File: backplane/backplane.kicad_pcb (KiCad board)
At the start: 2 copper layers, 150 x 150 mm, 14 parts

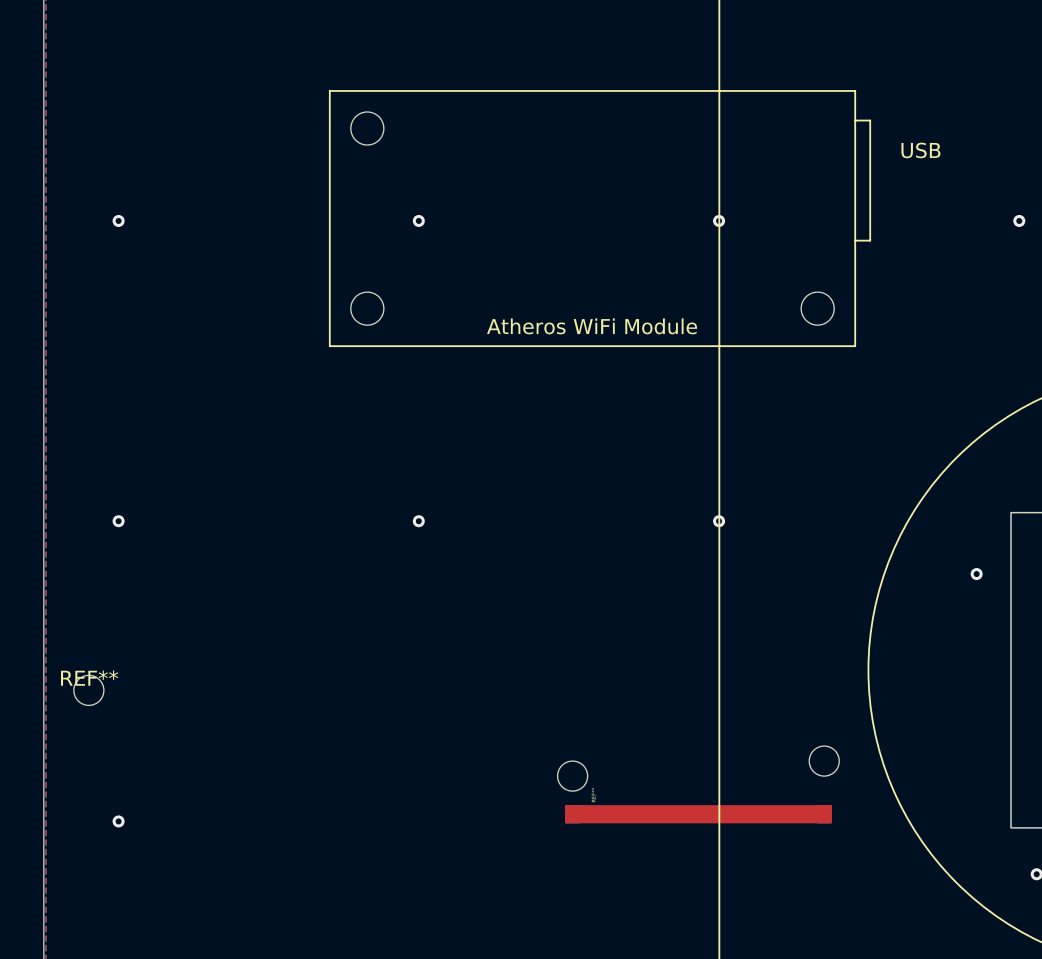
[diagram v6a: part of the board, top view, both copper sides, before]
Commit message: Adding major changes to transformer and others
Moved Atheros module out from under phone clamp for easier assembly.
Slot for antenna wire to feed through is now a edge cut.
Through-hole to GND plane on opposite end of transformer is now a SMD for
   a UFL connector.
Transformer clearance is now a copper trace isolating the microstrip.
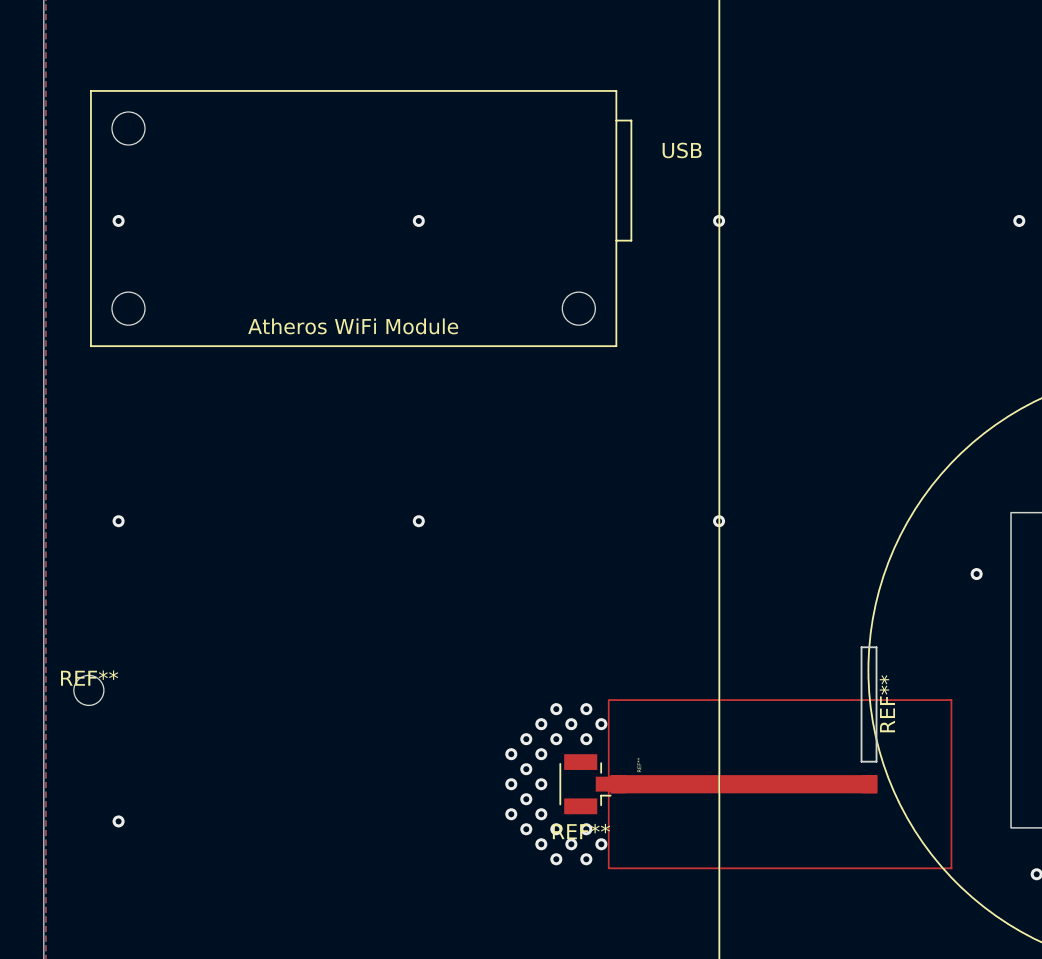
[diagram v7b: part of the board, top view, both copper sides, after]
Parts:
- added REF**: antenna-wire-slot, DxWiFi:antenna-wire-slot, F.Cu at (79.6, 107.7)
- added REF**: U.FL_Hirose_U.FL-R-SMT-1_Vertical, Connector_Coaxial:U.FL_Hirose_U.FL-R-SMT-1_Vertical, F.Cu at (59.1, 113.0)
- moved Atheros WiFi Module 15.9 mm to (26.0, 83.8)
- moved REF** 3.63 mm to (63.0, 113.0)
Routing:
- net Net-(L1-Pad1): vias 62 -> 86
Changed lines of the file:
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@@
     (thickness 1.6)
     (drawings 4)
-    (tracks 62)
+    (tracks 86)
     (zones 0)
-    (modules 14)
+    (modules 16)
     (nets 2)
   )
@@
     (mod_text_size 1 1)
     (mod_text_width 0.15)
-    (pad_size 0.8 0.8)
-    (pad_drill 0.4)
+    (pad_size 2.2 1.05)
+    (pad_drill 0)
     (pad_to_mask_clearance 0.051)
     (solder_mask_min_width 0.25)
@@
     (add_net "Net-(L1-Pad1)")
   )
-  (module muwave_stub (layer F.Cu)
-    (at 60 115 270)
-    (fp_text reference REF** (at -1.27 0.5 270) (layer F.SilkS)
+  (module DxWiFi:antenna-wire-slot (layer F.Cu)
+    (at 79.6 107.69 270)
+    (fp_text reference REF** (at 0 0.5 270) (layer F.SilkS)
+      (effects (font (size 1 1) (thickness 0.15)))
+    )
+    (fp_text value antenna-wire-slot (at 0 -0.5 270) (layer F.Fab)
+      (effects (font (size 1 1) (thickness 0.15)))
+    )
+    (fp_line (start 3.81 2.27) (end -3.81 2.27) (layer Edge.Cuts) (width 0.12))
+    (fp_line (start 3.81 1.27) (end 3.81 2.27) (layer Edge.Cuts) (width 0.12))
+    (fp_line (start -3.81 1.27) (end 3.81 1.27) (layer Edge.Cuts) (width 0.12))
+    (fp_line (start -3.81 1.27) (end -3.81 2.27) (layer Edge.Cuts) (width 0.12))
+  )
+  (module muwave_stub locked (layer F.Cu)
+    (at 63.03385 113 270)
+    (fp_text reference REF** (at -1.27 0.5 90) (layer F.SilkS)
       (effects (font (size 0.25 0.25) (thickness 0.05)))
     )
-    (fp_text value muwave_stub (at 0 -0.5 270) (layer F.Fab)
+    (fp_text value muwave_stub (at 0 -0.5 90) (layer F.Fab)
       (effects (font (size 0.25 0.25) (thickness 0.05)))
     )
-    (pad "" np_thru_hole circle (at -2.54 1.915 270) (size 2 2) (drill 2) (layers *.Cu *.Mask))
-    (pad "" np_thru_hole roundrect (at -3.54 -14.8473 270) (size 4 2) (drill 2) (layers *.Cu) (roundrect_rratio 0.25)
-      (clearance 0.5))
-    (pad 2 smd rect (at 0 1.915 270) (size 1.20938 1) (layers F.Cu F.Mask))
-    (pad 2 smd rect (at 0 -14.8473 270) (size 1.20938 1) (layers F.Cu F.Mask))
-    (pad 1 smd rect (at 0 0 270) (size 0.25 0.25) (layers B.Cu))
-    (pad 1 smd rect (at 0 -6.46615 270) (size 1.20938 17.7623) (layers F.Cu)
-      (clearance 12.6))
+    (fp_line (start -5.60469 2.54) (end 5.60469 2.54) (layer F.Cu) (width 0.12))
+    (fp_line (start 5.60469 -20.287299) (end 5.60469 2.475001) (layer F.Cu) (width 0.12))
+    (fp_line (start -5.60469 -20.287299) (end 5.60469 -20.287299) (layer F.Cu) (width 0.12))
+    (fp_line (start -5.60469 -20.287299) (end -5.60469 2.475001) (layer F.Cu) (width 0.12))
+    (pad 1 smd rect (at 0 -6.46615 270) (size 1.20938 17.7623) (layers F.Cu))
+    (pad 1 smd rect (at 0 -14.8473 270) (size 1.20938 1) (layers F.Cu F.Mask))
+    (pad 1 smd rect (at 0 1.915 270) (size 1.20938 1) (layers F.Cu F.Mask))
+  )
+  (module Connector_Coaxial:U.FL_Hirose_U.FL-R-SMT-1_Vertical (layer F.Cu)
+    (at 59.1 113 180)
+    (descr "Hirose U.FL Coaxial https://www.hirose.com/product/en/products/U.FL/U.FL-R-SMT-1%2810%29/")
+    (tags "Hirose U.FL Coaxial")
+    (attr smd)
+    (fp_text reference REF** (at 0.475 -3.2) (layer F.SilkS)
+      (effects (font (size 1 1) (thickness 0.15)))
+    )
+    (fp_text value U.FL_Hirose_U.FL-R-SMT-1_Vertical (at 0.475 3.2) (layer F.Fab)
+      (effects (font (size 1 1) (thickness 0.15)))
+    )
+    (fp_line (start -1.32 -1) (end -2.02 -1) (layer F.CrtYd) (width 0.05))
+    (fp_line (start -1.32 1.8) (end -1.32 1) (layer F.CrtYd) (width 0.05))
+    (fp_line (start -1.32 -1.8) (end -1.12 -1.8) (layer F.CrtYd) (width 0.05))
+    (fp_line (start -1.12 -1.8) (end -1.12 -2.5) (layer F.CrtYd) (width 0.05))
+    (fp_line (start 2.08 -2.5) (end -1.12 -2.5) (layer F.CrtYd) (width 0.05))
+    (fp_line (start -1.32 -1) (end -1.32 -1.8) (layer F.CrtYd) (width 0.05))
+    (fp_line (start 2.08 -1.8) (end 2.08 -2.5) (layer F.CrtYd) (width 0.05))
+    (fp_line (start 2.08 -1.8) (end 2.28 -1.8) (layer F.CrtYd) (width 0.05))
+    (fp_line (start -0.885 -1.4) (end -0.885 -0.76) (layer F.SilkS) (width 0.12))
+    (fp_line (start -0.425 1.5) (end -0.425 1.3) (layer F.Fab) (width 0.1))
+    (fp_line (start -0.425 1.3) (end -0.825 1.3) (layer F.Fab) (width 0.1))
+    (fp_line (start -0.825 0.3) (end -0.825 1.3) (layer F.Fab) (width 0.1))
+    (fp_line (start -1.075 0.3) (end -0.825 0.3) (layer F.Fab) (width 0.1))
+    (fp_line (start -1.075 0.3) (end -1.075 -0.15) (layer F.Fab) (width 0.1))
+    (fp_line (start -0.925 -0.3) (end -0.825 -0.3) (layer F.Fab) (width 0.1))
+    (fp_line (start -0.825 -0.3) (end -0.825 -1.3) (layer F.Fab) (width 0.1))
+    (fp_line (start -0.425 -1.5) (end -0.425 -1.3) (layer F.Fab) (width 0.1))
+    (fp_line (start -0.425 -1.3) (end -0.825 -1.3) (layer F.Fab) (width 0.1))
+    (fp_line (start -0.425 1.5) (end 1.375 1.5) (layer F.Fab) (width 0.1))
+    (fp_line (start 1.375 1.5) (end 1.375 1.3) (layer F.Fab) (width 0.1))
+    (fp_line (start 1.775 1.3) (end 1.375 1.3) (layer F.Fab) (width 0.1))
+    (fp_line (start 1.775 -1.3) (end 1.775 1.3) (layer F.Fab) (width 0.1))
+    (fp_line (start -0.425 -1.5) (end 1.375 -1.5) (layer F.Fab) (width 0.1))
+    (fp_line (start 1.375 -1.5) (end 1.375 -1.3) (layer F.Fab) (width 0.1))
+    (fp_line (start 1.775 -1.3) (end 1.375 -1.3) (layer F.Fab) (width 0.1))
+    (fp_line (start -0.925 -0.3) (end -1.075 -0.15) (layer F.Fab) (width 0.1))
+    (fp_line (start -0.885 1.4) (end -0.885 0.76) (layer F.SilkS) (width 0.12))
+    (fp_line (start -0.885 -0.76) (end -1.515 -0.76) (layer F.SilkS) (width 0.12))
+    (fp_line (start 1.835 -1.35) (end 1.835 1.35) (layer F.SilkS) (width 0.12))
+    (fp_line (start 2.08 2.5) (end -1.12 2.5) (layer F.CrtYd) (width 0.05))
+    (fp_line (start -1.12 2.5) (end -1.12 1.8) (layer F.CrtYd) (width 0.05))
+    (fp_line (start -1.32 1.8) (end -1.12 1.8) (layer F.CrtYd) (width 0.05))
+    (fp_line (start 2.28 1.8) (end 2.28 -1.8) (layer F.CrtYd) (width 0.05))
+    (fp_line (start 2.08 2.5) (end 2.08 1.8) (layer F.CrtYd) (width 0.05))
+    (fp_line (start 2.08 1.8) (end 2.28 1.8) (layer F.CrtYd) (width 0.05))
+    (fp_line (start -1.32 1) (end -2.02 1) (layer F.CrtYd) (width 0.05))
+    (fp_line (start -2.02 1) (end -2.02 -1) (layer F.CrtYd) (width 0.05))
+    (fp_text user %R (at 0.475 0 90) (layer F.Fab)
+      (effects (font (size 0.6 0.6) (thickness 0.09)))
+    )
+    (pad 2 smd rect (at 0.475 -1.475 180) (size 2.2 1.05) (layers F.Cu F.Paste F.Mask)
+      (net 1 "Net-(L1-Pad1)"))
+    (pad 1 smd rect (at -1.05 0 180) (size 1.05 1) (layers F.Cu F.Paste F.Mask))
+    (pad 2 smd rect (at 0.475 1.475 180) (size 2.2 1.05) (layers F.Cu F.Paste F.Mask)
+      (net 1 "Net-(L1-Pad1)"))
+    (model ${KISYS3DMOD}/Connector_Coaxial.3dshapes/U.FL_Hirose_U.FL-R-SMT-1_Vertical.wrl
+      (offset (xyz 0.4749999928262157 0 0))
+      (scale (xyz 1 1 1))
+      (rotate (xyz 0 0 0))
+    )
   )
   (module DxWiFi:logo_oresat (layer F.Cu)
@@
   )
   (module DxWiFi:Atheros (layer F.Cu)
-    (at 41.91 83.82)
+    (at 26 83.82)
     (fp_text reference "Atheros WiFi Module" (at 17.5 -3.5) (layer F.Fab) hide
       (effects (font (size 1 1) (thickness 0.15)))
@@
   (gr_line (start 172.86 30.48) (end 172.86 180.48) (layer Edge.Cuts) (width 0.05))
   (gr_line (start 22.86 30.48) (end 172.86 30.48) (layer Edge.Cuts) (width 0.05))
+  (via (at 60 109) (size 0.8) (drill 0.4) (layers F.Cu B.Cu) (net 1))
+  (via (at 59 110) (size 0.8) (drill 0.4) (layers F.Cu B.Cu) (net 1))
+  (via (at 59 108) (size 0.8) (drill 0.4) (layers F.Cu B.Cu) (net 1))
+  (via (at 58 109) (size 0.8) (drill 0.4) (layers F.Cu B.Cu) (net 1))
+  (via (at 57 108) (size 0.8) (drill 0.4) (layers F.Cu B.Cu) (net 1))
+  (via (at 57 110) (size 0.8) (drill 0.4) (layers F.Cu B.Cu) (net 1))
+  (via (at 56 109) (size 0.8) (drill 0.4) (layers F.Cu B.Cu) (net 1))
+  (via (at 56 111) (size 0.8) (drill 0.4) (layers F.Cu B.Cu) (net 1))
+  (via (at 55 112) (size 0.8) (drill 0.4) (layers F.Cu B.Cu) (net 1))
+  (via (at 56 113) (size 0.8) (drill 0.4) (layers F.Cu B.Cu) (net 1))
+  (via (at 55 114) (size 0.8) (drill 0.4) (layers F.Cu B.Cu) (net 1))
+  (via (at 56 115) (size 0.8) (drill 0.4) (layers F.Cu B.Cu) (net 1))
+  (via (at 55 116) (size 0.8) (drill 0.4) (layers F.Cu B.Cu) (net 1))
+  (via (at 56 117) (size 0.8) (drill 0.4) (layers F.Cu B.Cu) (net 1))
+  (via (at 57 116) (size 0.8) (drill 0.4) (layers F.Cu B.Cu) (net 1))
+  (via (at 58 117) (size 0.8) (drill 0.4) (layers F.Cu B.Cu) (net 1))
+  (via (at 59 116) (size 0.8) (drill 0.4) (layers F.Cu B.Cu) (net 1))
+  (via (at 60 117) (size 0.8) (drill 0.4) (layers F.Cu B.Cu) (net 1))
+  (via (at 59 118) (size 0.8) (drill 0.4) (layers F.Cu B.Cu) (net 1))
+  (via (at 57 118) (size 0.8) (drill 0.4) (layers F.Cu B.Cu) (net 1))
+  (via (at 54 111) (size 0.8) (drill 0.4) (layers F.Cu B.Cu) (net 1))
+  (via (at 54 113) (size 0.8) (drill 0.4) (layers F.Cu B.Cu) (net 1))
+  (via (at 54 115) (size 0.8) (drill 0.4) (layers F.Cu B.Cu) (net 1))
+  (via (at 55 110) (size 0.8) (drill 0.4) (layers F.Cu B.Cu) (net 1))
   (via (at 167.84 175.48) (size 0.8) (drill 0.4) (layers F.Cu B.Cu) (net 1))
   (via (at 147.84 175.48) (size 0.8) (drill 0.4) (layers F.Cu B.Cu) (net 1))

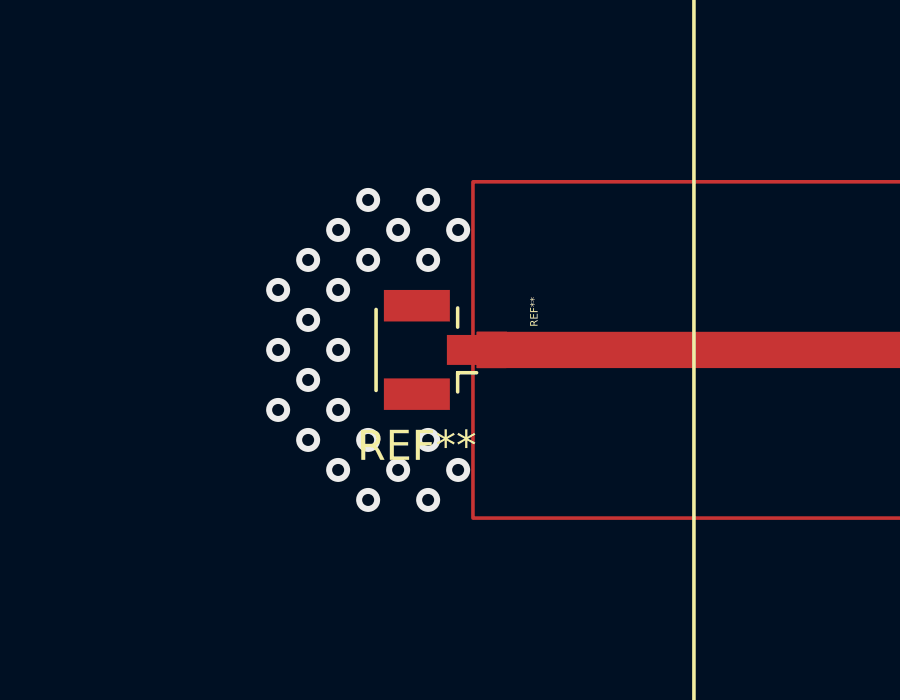
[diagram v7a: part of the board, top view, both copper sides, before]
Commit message: Disconnected transformer clearance border from microstrip
Gerber files have also been updated to reflect the current layout
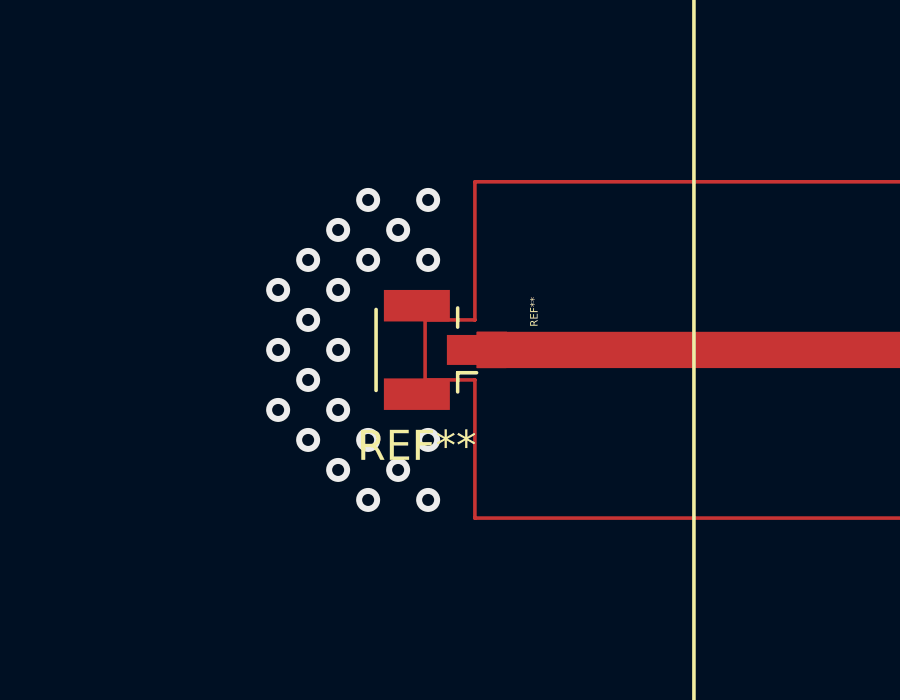
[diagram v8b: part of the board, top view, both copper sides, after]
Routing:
- net Net-(L1-Pad1): vias 86 -> 84
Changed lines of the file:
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@@
     (thickness 1.6)
     (drawings 4)
-    (tracks 86)
+    (tracks 84)
     (zones 0)
     (modules 16)
@@
     (add_net "Net-(L1-Pad1)")
   )
+  (module muwave_stub locked (layer F.Cu)
+    (at 63.03385 113 270)
+    (fp_text reference REF** (at -1.27 0.5 270) (layer F.SilkS)
+      (effects (font (size 0.25 0.25) (thickness 0.05)))
+    )
+    (fp_text value muwave_stub (at 0 -0.5 270) (layer F.Fab)
+      (effects (font (size 0.25 0.25) (thickness 0.05)))
+    )
+    (fp_line (start -1 2.475001) (end -1 4.135001) (layer F.Cu) (width 0.12))
+    (fp_line (start 1 2.475001) (end 5.60469 2.475001) (layer F.Cu) (width 0.12))
+    (fp_line (start -5.60469 -20.287299) (end -5.60469 2.475001) (layer F.Cu) (width 0.12))
+    (fp_line (start -5.60469 -20.287299) (end 5.60469 -20.287299) (layer F.Cu) (width 0.12))
+    (fp_line (start 5.60469 -20.287299) (end 5.60469 2.475001) (layer F.Cu) (width 0.12))
+    (fp_line (start -5.60469 2.475001) (end -1 2.475001) (layer F.Cu) (width 0.12))
+    (fp_line (start 1 2.475001) (end 1 4.135001) (layer F.Cu) (width 0.12))
+    (fp_line (start -1 4.135001) (end 1 4.135001) (layer F.Cu) (width 0.12))
+    (pad 1 smd rect (at 0 1.915 270) (size 1.20938 1) (layers F.Cu F.Mask))
+    (pad 1 smd rect (at 0 -14.8473 270) (size 1.20938 1) (layers F.Cu F.Mask))
+    (pad 1 smd rect (at 0 -6.46615 270) (size 1.20938 17.7623) (layers F.Cu))
+  )
   (module DxWiFi:antenna-wire-slot (layer F.Cu)
     (at 79.6 107.69 270)
@@
     (fp_line (start -3.81 1.27) (end 3.81 1.27) (layer Edge.Cuts) (width 0.12))
     (fp_line (start -3.81 1.27) (end -3.81 2.27) (layer Edge.Cuts) (width 0.12))
-  )
-  (module muwave_stub locked (layer F.Cu)
-    (at 63.03385 113 270)
-    (fp_text reference REF** (at -1.27 0.5 90) (layer F.SilkS)
-      (effects (font (size 0.25 0.25) (thickness 0.05)))
-    )
-    (fp_text value muwave_stub (at 0 -0.5 90) (layer F.Fab)
-      (effects (font (size 0.25 0.25) (thickness 0.05)))
-    )
-    (fp_line (start -5.60469 2.54) (end 5.60469 2.54) (layer F.Cu) (width 0.12))
-    (fp_line (start 5.60469 -20.287299) (end 5.60469 2.475001) (layer F.Cu) (width 0.12))
-    (fp_line (start -5.60469 -20.287299) (end 5.60469 -20.287299) (layer F.Cu) (width 0.12))
-    (fp_line (start -5.60469 -20.287299) (end -5.60469 2.475001) (layer F.Cu) (width 0.12))
-    (pad 1 smd rect (at 0 -6.46615 270) (size 1.20938 17.7623) (layers F.Cu))
-    (pad 1 smd rect (at 0 -14.8473 270) (size 1.20938 1) (layers F.Cu F.Mask))
-    (pad 1 smd rect (at 0 1.915 270) (size 1.20938 1) (layers F.Cu F.Mask))
   )
   (module Connector_Coaxial:U.FL_Hirose_U.FL-R-SMT-1_Vertical (layer F.Cu)
@@
   (gr_line (start 172.86 30.48) (end 172.86 180.48) (layer Edge.Cuts) (width 0.05))
   (gr_line (start 22.86 30.48) (end 172.86 30.48) (layer Edge.Cuts) (width 0.05))
-  (via (at 60 109) (size 0.8) (drill 0.4) (layers F.Cu B.Cu) (net 1))
   (via (at 59 110) (size 0.8) (drill 0.4) (layers F.Cu B.Cu) (net 1))
   (via (at 59 108) (size 0.8) (drill 0.4) (layers F.Cu B.Cu) (net 1))
@@
   (via (at 58 117) (size 0.8) (drill 0.4) (layers F.Cu B.Cu) (net 1))
   (via (at 59 116) (size 0.8) (drill 0.4) (layers F.Cu B.Cu) (net 1))
-  (via (at 60 117) (size 0.8) (drill 0.4) (layers F.Cu B.Cu) (net 1))
   (via (at 59 118) (size 0.8) (drill 0.4) (layers F.Cu B.Cu) (net 1))
   (via (at 57 118) (size 0.8) (drill 0.4) (layers F.Cu B.Cu) (net 1))
